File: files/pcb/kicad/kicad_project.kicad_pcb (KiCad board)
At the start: 2 copper layers, 100 x 60.5 mm, 2 parts, among them IC1 ICM7555CD, IC2 ICM7555CD

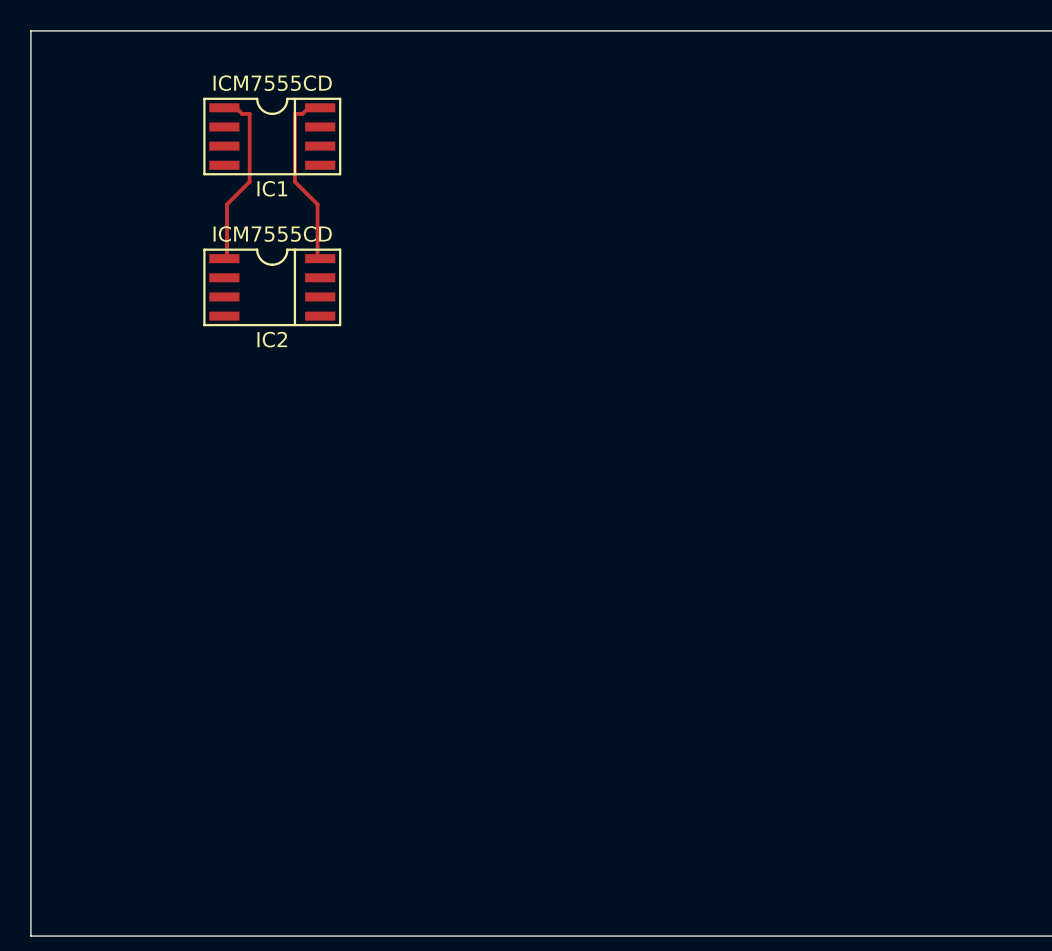
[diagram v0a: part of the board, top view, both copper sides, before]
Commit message: 回路更新
マイコン周り作成、各子階層シートを追加
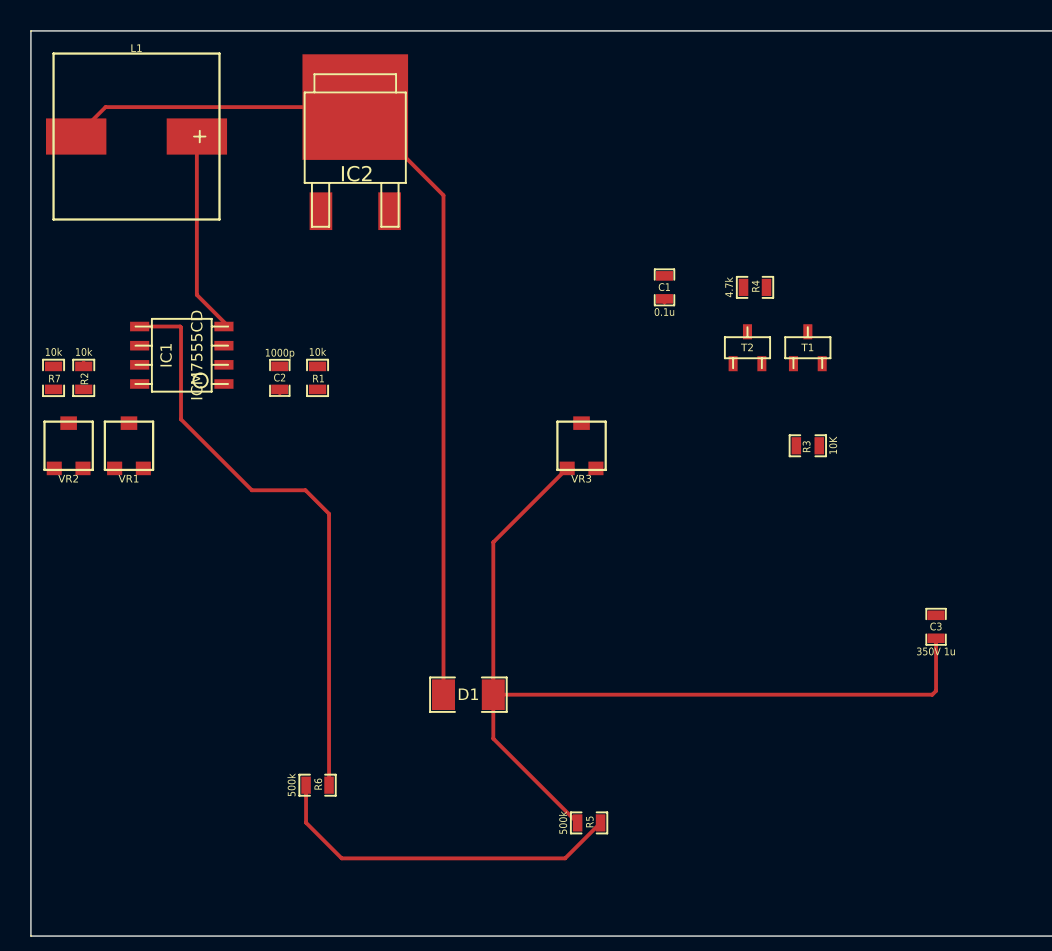
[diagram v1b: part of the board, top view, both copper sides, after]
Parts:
- added C1: 0.1u, SM0603_Capa, F.Cu at (67.0, 36.0)
- added C2: 1000p, SM0603_Capa, F.Cu at (41.5, 42.0)
- added C3: 350V 1u, SM0603_Capa, F.Cu at (85.0, 58.5)
- added D1: DIODE, SM1206, F.Cu at (54.0, 63.0)
- added L1: 220uH, smd10x10, F.Cu at (32.0, 26.0)
- added R1: 10k, SM0603_Resistor, F.Cu at (44.0, 42.0)
- added R2: 10k, SM0603_Resistor, F.Cu at (28.5, 42.0)
- added R3: 10K, SM0603_Resistor, F.Cu at (76.5, 46.5)
- added R4: 4.7k, SM0603_Resistor, F.Cu at (73.0, 36.0)
- added R5: 500k, SM0603_Resistor, F.Cu at (62.0, 71.5)
- added R6: 500k, SM0603_Resistor, F.Cu at (44.0, 69.0)
- added R7: 10k, SM0603_Resistor, F.Cu at (26.5, 42.0)
- added T1: 2SC, sot23, F.Cu at (76.5, 40.0)
- added T2: 2SA, sot23, F.Cu at (72.5, 40.0)
- added VR1: 100k, SMD_VOLUME, F.Cu at (31.5, 46.5)
- added VR2: 10k, SMD_VOLUME, F.Cu at (27.5, 46.5)
- added VR3: VOLUME, SMD_VOLUME, F.Cu at (61.5, 46.5)
- IC1: footprint ICM7555CD -> so-8
- IC2: value ICM7555CD -> FET; footprint ICM7555CD -> sot428
- moved IC1 15.7 mm to (35.0, 40.5), turned to 90 degrees
- moved IC2 10.1 mm to (46.5, 27.5)
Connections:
- IC1 pad 1: +5V -> GND
- IC1 pad 2: (no net) -> N-0000015
- IC1 pad 3: (no net) -> N-0000014
- IC1 pad 4: (no net) -> +9V
- IC1 pad 5: (no net) -> N-0000010
- IC1 pad 6: (no net) -> N-0000011
- IC1 pad 7: (no net) -> N-000009
- IC1 pad 8: N-000001 -> +9V
- IC2 pad 1: +5V -> N-000005
- IC2 pad 2: (no net) -> N-000004
- IC2 pad 3: (no net) -> GND
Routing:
- net /nixie/170V: track 0.00 -> 61.3 mm
- net N-000004: track 0.00 -> 60.8 mm
- net N-0000010: track 0.00 -> 39.7 mm
- net N-000002: track 0.00 -> 24.0 mm
- net +9V: track 0.00 -> 14.0 mm
- net N-000001: track 12.2 -> 0.00 mm
- net +5V: track 12.2 -> 0.00 mm
- net GND: track 0.00 -> 1.87 mm

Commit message: 回路図ERC途中
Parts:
- added 200k1, 200k2: N/A, SM0603, F.Cu at (125.1, 79.6)
- added C10: 1000p, SM0603_Capa, F.Cu at (125.1, 79.6)
- added C5: 25V 10u, SM1206, F.Cu at (122.0, 72.8)
- added C6, C7, C8: 0.1u, SM0603_Capa, F.Cu at (125.1, 79.6)
- added C9: 25V 10u, SM1206, F.Cu at (121.2, 75.4)
- added T3: 2SA, TO92, F.Cu at (113.1, 74.2)
- C2: value 1000p -> 10u
- C3: value 350V 1u -> 22p
- IC1: value ICM7555CD -> ATMEGA328-A
- IC2: value FET -> 3-TERMINAL_REGULATOR
- R1: value 10k -> R
- R2: value 10k -> 1k
- R3: value 10K -> 10k
- R4: value 4.7k -> R
- R5: value 500k -> R
- R6: value 500k -> 10k
- T2: value 2SA -> 2SC
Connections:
- C1 pad 1: GND -> N-0000016
- C1 pad 2: +9V -> GND
- C2 pad 1: N-0000015 -> N-0000012
- C3 pad 1: /nixie/170V -> N-000005
- D1 pad 1: N-000004 -> N-0000012
- D1 pad 2: /nixie/170V -> +5V
- IC1 pad 1: GND -> /Sheet53F8CD20/D-
- IC1 pad 2: N-0000015 -> /Sheet53F9209C/out
- IC1 pad 3: N-0000014 -> GND
- IC1 pad 4: +9V -> +5V
- IC1 pad 5: N-0000010 -> GND
- IC1 pad 6: N-0000011 -> +5V
- IC1 pad 7: N-000009 -> N-000008
- IC1 pad 8: +9V -> N-000005
- IC2 pad 1: N-000005 -> (no net)
- IC2 pad 2: N-000004 -> (no net)
- IC2 pad 3: GND -> (no net)
- L1 pad 1: +9V -> N-0000069
- L1 pad 2: N-000004 -> N-0000059
- R1 pad 1: N-000009 -> +5V
- R1 pad 2: +9V -> N-0000016
- R2 pad 1: N-0000011 -> N-0000018
- R2 pad 2: N-000009 -> N-0000012
- R3 pad 1: N-000005 -> +5V
- R3 pad 2: N-0000014 -> N-0000012
- R4 pad 1: +9V -> +5V
- R4 pad 2: N-000006 -> /Sheet53F905A8/SCL
- R5 pad 1: /nixie/170V -> +5V
- R5 pad 2: N-000002 -> /Sheet53F905A8/SDA
- R6 pad 1: N-000002 -> +5V
- R6 pad 2: N-0000010 -> N-0000046
- R7 pad 1: N-0000010 -> GND
- R7 pad 2: N-000003 -> /Sheet53F8BA4D/out
- T1 pad 1: N-0000014 -> N-0000055
- T1 pad 2: N-000006 -> N-0000065
- T1 pad 3: N-000005 -> GND
- T2 pad 1: N-0000014 -> N-0000061
- T2 pad 2: GND -> N-0000060
- T2 pad 3: N-000005 -> N-0000062
- VR1 pad 1: N-0000011 -> N-0000066
- VR1 pad 2: N-0000015 -> N-0000068
- VR1 pad 3: N-0000015 -> N-0000068
- VR2 pad 1: N-000003 -> N-0000063
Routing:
- net +5V: track 0.00 -> 74.5 mm
- net N-000004: track 60.8 -> 0.00 mm
- net N-0000012: track 0.00 -> 58.0 mm
- net /nixie/170V: track 61.3 -> 6.92 mm
- net N-0000010: track 39.7 -> 0.00 mm
- net N-000002: track 24.0 -> 0.00 mm
- net GND: track 1.87 -> 22.4 mm
- net N-0000046: track 0.00 -> 18.0 mm
- net +9V: track 14.0 -> 0.00 mm
- net N-0000069: track 0.00 -> 10.5 mm
- net N-000005: track 0.30 -> 3.96 mm
- net /Sheet53F905A8/SDA: track 0.00 -> 3.32 mm
- net N-0000059: track 0.00 -> 2.76 mm

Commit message: 部品リスト完了、PCBに部品を配置
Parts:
- removed 200k1, 200k2: N/A, SM0603
- removed VR3: VOLUME, SMD_VOLUME
- added C11: 25V 10u, SM0805, F.Cu at (256.0, 133.0)
- added C12: 1000p, SM0603_Capa, F.Cu at (229.5, 171.0)
- added C13: 350V 1u, my_SMD5750, F.Cu at (214.5, 124.0)
- added C14: 5.5V 0.1F, my_double_layer_capacitor, F.Cu at (210.5, 151.5)
- added C15: 0.1u, SM0603_Capa, F.Cu at (231.0, 180.0)
- added C16: 0.1u, SM0603_Capa, F.Cu at (231.0, 163.0)
- added C17: 0.1u, SM0603_Capa, F.Cu at (245.0, 179.5)
- added C18: 0.1u, SM0603_Capa, F.Cu at (253.0, 185.0)
- added C19: 0.1u, SM0603_Capa, F.Cu at (236.0, 180.0)
- added C4: 22p, SM0603_Capa, F.Cu at (236.0, 177.5)
- added CON1: USB_MINI_B, my_usb_mini_b, F.Cu at (163.0, 111.5)
- added D2: DIODE, SM1206POL, F.Cu at (232.5, 125.0)
- added D3: DIODE, SM0805, F.Cu at (249.0, 175.0)
- added D4: DIODE, SM0805, F.Cu at (160.0, 118.5)
- added D5: DIODE, SM0805, F.Cu at (242.5, 151.0)
- added F1: FUSE, SM1206, F.Cu at (223.5, 134.5)
- added IC10: FET, my_sot428, F.Cu at (241.5, 122.0)
- added IC11: DS1307, so-8, F.Cu at (245.5, 133.0)
- added IC12: IC_8PIN, my_dip8, F.Cu at (192.5, 118.5)
- added IC13: AM2321, my_am2321, F.Cu at (202.0, 131.5)
- added IC3: IC_4PIN, my_dip4, F.Cu at (209.0, 167.0)
- added IC4: IC_4PIN, my_dip4, F.Cu at (211.5, 181.5)
- added IC5: SN74141_K155NA, my_dip16, F.Cu at (172.0, 172.0)
- added IC6: TLP627-4, my_dip16, F.Cu at (195.0, 178.0)
- added IC7: TLP627-4, my_dip16, F.Cu at (172.0, 178.0)
- added IC8: MY_3_TERMINAL_REGULATOR, my_SOT223, F.Cu at (226.5, 118.0)
- added IC9: ICM7555CD, so-8, F.Cu at (219.5, 103.5)
- added K1: CONN_3, my_3pin, F.Cu at (199.5, 188.5)
- added K2: CONN_3, my_3pin, F.Cu at (190.0, 189.0)
- added K3: CONN_3, my_3pin, F.Cu at (241.5, 184.5)
- added K4: CONN_3, my_3pin, F.Cu at (236.5, 185.5)
- added P1: CONN_6, my_connector_6, F.Cu at (196.5, 144.5)
- added PD1: PHOTO_DIODE, my_photo_diode, F.Cu at (226.0, 127.0)
- added R10: 500k, SM0805, F.Cu at (241.5, 176.5)
- added R11: 10k, SM0805, F.Cu at (237.0, 155.5)
- added R12: 10k, SM0805, F.Cu at (223.5, 148.0)
- added R13: 10k, SM0805, F.Cu at (219.0, 145.0)
- added R14: 10k, SM0805, F.Cu at (220.5, 115.5)
- added R15: 10K, SM0805, F.Cu at (247.5, 146.5)
- added R16: 4.7k, SM0805, F.Cu at (230.0, 158.5)
- added R17: 500k, SM0805, F.Cu at (232.0, 167.0)
- added R18: 500k, SM0805, F.Cu at (235.5, 172.5)
- added R19: 10k, SM0805, F.Cu at (251.5, 153.0)
- added R20: 68, SM0805, F.Cu at (191.5, 153.0)
- added R21: 68, SM0805, F.Cu at (165.0, 128.0)
- added R22: 2K, SM0805, F.Cu at (172.0, 117.5)
- added R23: NC, SM0805, F.Cu at (222.0, 154.5)
- added R24: 10k, SM0805, F.Cu at (217.5, 164.5)
- added R25: 10k, SM0805, F.Cu at (249.5, 178.0)
- added R26: 10k, SM0805, F.Cu at (249.0, 180.5)
- added R27: 3.3k, SM0805, F.Cu at (231.0, 174.5)
- added R28: 7.5k, SM0805, F.Cu at (237.5, 175.0)
- added R29: 10k, SM0805, F.Cu at (236.5, 162.5)
- added R30: N/A, SM0805, F.Cu at (200.5, 181.0)
- added R31: N/A, SM0805, F.Cu at (225.5, 165.0)
- added R8: 10k, SM0805, F.Cu at (237.5, 150.0)
- added R9: 500k, SM0805, F.Cu at (222.0, 167.5)
- added SW1: SW_PUSH, my_tact_switch, F.Cu at (205.5, 115.5)
- added SW2: EVQWK, my_rotary_switch, F.Cu at (180.0, 156.5)
- added SW3: SW_PUSH, my_tact_switch, F.Cu at (196.0, 115.5)
- added SW4: SW_PUSH, my_tact_switch, F.Cu at (187.0, 115.5)
- added SW5: SW_PUSH, my_tact_switch, F.Cu at (177.5, 115.5)
- added U1: NEON, my_neon, F.Cu at (190.0, 192.0)
- added U10: NIXIE_IN_16, my_nixie, F.Cu at (181.5, 196.0)
- added U11: DC_JACK, my_dcjack, F.Cu at (161.5, 156.5)
- added U12: LOAD, my_sounder, F.Cu at (248.0, 165.5)
- added U13: remocon, my_remocon, F.Cu at (181.5, 123.0)
- added U14: napion, my_napion, F.Cu at (169.5, 121.0)
- added U2: NEON, my_neon, F.Cu at (195.0, 182.5)
- added U3: NEON, my_neon, F.Cu at (232.0, 186.0)
- added U4: NEON, my_neon, F.Cu at (228.5, 184.0)
- added U5: NIXIE_IN_16, my_nixie, F.Cu at (243.5, 196.0)
- added U6: NIXIE_IN_16, my_nixie, F.Cu at (213.5, 196.5)
- added U7: NIXIE_IN_16, my_nixie, F.Cu at (166.5, 196.0)
- added U8: NIXIE_IN_16, my_nixie, F.Cu at (229.0, 196.5)
- added U9: NIXIE_IN_16, my_nixie, F.Cu at (198.0, 196.5)
- added X1: 12MHz, my_crystal, F.Cu at (190.0, 163.0)
- added X2: 32.768kHz, my_crystal_32p768, F.Cu at (223.0, 182.5)
- C10: value 1000p -> 0.1u
- C2: value 10u -> 0.1u
- C3: value 22p -> 10u; footprint SM0603_Capa -> SM0805
- C5: value 25V 10u -> 22p; footprint SM1206 -> SM0603_Capa
- C7: value 0.1u -> 25V 10u; footprint SM0603_Capa -> SM0805
- C9: value 25V 10u -> 0.1u; footprint SM1206 -> SM0603_Capa
- D1: footprint SM1206 -> SM0805
- IC1: footprint so-8 -> TQFP32
- IC2: value 3-TERMINAL_REGULATOR -> IC_16PIN; footprint sot428 -> my_so16
- L1: footprint smd10x10 -> my_inductor
- R1: value R -> 510; footprint SM0603_Resistor -> SM0805
- R2, R3, R7: footprint SM0603_Resistor -> SM0805
- R4, R5: value R -> 10k; footprint SM0603_Resistor -> SM0805
- R6: value 10k -> 330; footprint SM0603_Resistor -> SM0805
- T1, T2: footprint sot23 -> SOT23
- T3: footprint TO92 -> SOT23
- VR1, VR2: footprint SMD_VOLUME -> my_SMD_VR
- moved R2 233.6 mm to (219.5, 176.5), turned to 0 degrees
- moved C2 233.5 mm to (237.5, 169.0), turned to 0 degrees
- moved R7 231.2 mm to (219.0, 170.0), turned to 180 degrees
- moved R6 226.6 mm to (244.5, 174.5), turned to 180 degrees
- moved VR2 224.5 mm to (235.5, 131.0), turned to 90 degrees
- moved R1 217.1 mm to (231.5, 151.5), turned to 0 degrees
- moved L1 212.0 mm to (228.5, 105.5), turned to 90 degrees
- moved D1 205.8 mm to (227.0, 174.5)
- moved IC2 203.7 mm to (191.5, 170.5), turned to 180 degrees
- moved IC1 202.8 mm to (198.5, 160.5), turned to 0 degrees
- moved C1 200.2 mm to (234.0, 146.5), turned to 0 degrees
- moved VR1 196.9 mm to (217.5, 111.0)
- moved R3 193.8 mm to (225.0, 171.0)
- moved R4 187.7 mm to (225.5, 145.5)
- moved T1 173.7 mm to (231.5, 118.5)
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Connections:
- C1 pad 1: N-0000016 -> N-0000018
- C10 pad 1: N-0000068 -> GND
- C10 pad 2: GND -> N-0000063
- C2 pad 1: N-0000012 -> +5V
- C3 pad 1: N-000005 -> N-000004
- C5 pad 1: N-0000069 -> N-000003
- C6 pad 1: N-0000069 -> GND
- C6 pad 2: GND -> +5V
- C7 pad 1: +5V -> N-0000063
- C8 pad 1: GND -> N-0000063
- C8 pad 2: N-0000069 -> GND
- D1 pad 1: N-0000012 -> N-000004
- IC1 pad 7: N-000008 -> N-000003
- IC1 pad 8: N-000005 -> N-0000011
- IC2 pad 1: (no net) -> /PB0
- IC2 pad 2: (no net) -> /PB1
- IC2 pad 3: (no net) -> /PB2
- L1 pad 1: N-0000069 -> N-0000063
- R1 pad 2: N-0000016 -> N-0000018
- R2 pad 1: N-0000018 -> /RESET
- R2 pad 2: N-0000012 -> N-000004
- R3 pad 2: N-0000012 -> N-000004
- R7 pad 1: GND -> +5V
- R7 pad 2: /Sheet53F8BA4D/out -> N-0000026
- VR1 pad 2: N-0000068 -> N-0000055
- VR1 pad 3: N-0000068 -> N-0000055
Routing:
- net +5V: track 74.5 -> 0.00 mm
- net N-0000012: track 58.0 -> 0.00 mm
- net GND: track 22.4 -> 0.00 mm
- net N-0000047: track 18.0 -> 0.00 mm
- net N-0000069: track 10.5 -> 0.00 mm
- net /nixie/170V: track 6.92 -> 0.00 mm
- net N-000005: track 3.96 -> 0.00 mm
- net /Sheet53F905A8/SDA: track 3.32 -> 0.00 mm
- net N-0000062: track 2.76 -> 0.00 mm
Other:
- board size 100 x 60.5 mm -> 100 x 99 mm

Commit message: PCB更新
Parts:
- added U15: MY_PIN52, my_pin52, F.Cu at (255.0, 118.0)
- added U16: MY_PIN52, my_pin52, F.Cu at (163.5, 148.0)
- added U17: MY_PIN52, my_pin52, F.Cu at (164.0, 118.5)
- added U18: MY_PIN52, my_pin52, F.Cu at (255.0, 148.5)
- added my_drill_3mm: VAL**, my_drill_3mm, F.Cu at (162.5, 130.5)
- added my_drill_3mm: VAL**, my_drill_3mm, F.Cu at (162.0, 106.0)
- added my_drill_3mm: VAL**, my_drill_3mm, F.Cu at (256.5, 131.0)
- added my_drill_3mm: VAL**, my_drill_3mm, F.Cu at (256.5, 106.5)
- added my_drill_3mm: VAL**, my_drill_3mm, F.Cu at (256.0, 138.5)
- added my_drill_3mm: VAL**, my_drill_3mm, F.Cu at (256.0, 159.5)
- added my_drill_3mm: VAL**, my_drill_3mm, F.Cu at (162.0, 157.5)
- added my_drill_3mm: VAL**, my_drill_3mm, F.Cu at (162.0, 138.0)
- IC12: value IC_8PIN -> LPS331AP
- moved U1 100.6 mm to (185.0, 91.5)
- moved K2 100.3 mm to (166.5, 91.5)
- moved U3 97.6 mm to (214.5, 90.0)
- moved K4 96.0 mm to (223.0, 90.5)
- moved U4 95.3 mm to (207.5, 91.0)
- moved U2 93.5 mm to (178.5, 90.5)
- moved U12 87.3 mm to (179.0, 112.0)
- moved D4 70.0 mm to (225.0, 144.5), turned to 270 degrees
- moved X2 61.5 mm to (197.5, 126.5), turned to 90 degrees
- moved R21 61.0 mm to (222.5, 148.5)
- moved F1 57.2 mm to (169.5, 153.5), turned to 270 degrees
- moved R22 57.1 mm to (220.0, 148.5)
- moved IC2 54.2 mm to (245.5, 165.5)
- moved X1 48.7 mm to (207.5, 117.5)
- moved C8 47.5 mm to (242.0, 139.5), turned to 270 degrees
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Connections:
- K2 pad 1: N-0000082 -> N-00000121
- K4 pad 1: N-0000079 -> N-00000118
- R30 pad 1: N-0000082 -> /nixie/Sheet53F9F7BA/colon_l
- R31 pad 1: N-0000079 -> /nixie/Sheet53F9F7BA/colon_r
- U1 pad 2: N-0000082 -> N-00000121
- U2 pad 2: N-0000082 -> N-00000121
- U3 pad 2: N-0000079 -> N-00000118
- U4 pad 2: N-0000079 -> N-00000118
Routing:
- net +5V: track 0.00 -> 264.3 mm, vias 0 -> 5
- net GND: track 0.00 -> 258.3 mm, vias 0 -> 5
- net /nixie/Sheet53F9F7BA/dot_cathode_r: track 0.00 -> 180.5 mm
- net N-0000091: track 0.00 -> 124.6 mm, vias 0 -> 4
- net /nixie/Sheet53F9F7BA/dot_cathode_l: track 0.00 -> 107.9 mm
- net /nixie/N9: track 0.00 -> 106.7 mm, vias 0 -> 2
- net /nixie/N2: track 0.00 -> 100.4 mm, vias 0 -> 4
- net /nixie/N7: track 0.00 -> 90.0 mm, vias 0 -> 2
- net /nixie/N1: track 0.00 -> 85.5 mm, vias 0 -> 1
- net /nixie/N4: track 0.00 -> 81.5 mm, vias 0 -> 2
- net /nixie/N0: track 0.00 -> 76.5 mm
- net /nixie/N3: track 0.00 -> 76.0 mm, vias 0 -> 1
- net /nixie/N8: track 0.00 -> 76.0 mm
- net /nixie/N5: track 0.00 -> 69.6 mm, vias 0 -> 1
- net /Sheet53F9209C/out: track 0.00 -> 60.0 mm, vias 0 -> 2
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- added copper zone on B.Cu, net GND
- added copper zone on F.Cu, net GND
- added copper zone on B.Cu, net N-00000117
- added copper zone on F.Cu, net N-00000117
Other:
- board size 100 x 99 mm -> 100 x 102 mm

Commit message: PCB
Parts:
- removed my_drill_3mm (x8): VAL**, my_drill_3mm
- added my_M3_screw: VAL**, my_M3_screw, F.Cu at (257.6, 181.5)
- added my_M3_screw: VAL**, my_M3_screw, F.Cu at (257.5, 109.6)
- added my_M3_screw: VAL**, my_M3_screw, F.Cu at (164.5, 109.6)
- added my_M3_screw: VAL**, my_M3_screw, F.Cu at (164.6, 181.5)
- added my_M3_screw: VAL**, my_M3_screw, F.Cu at (164.5, 141.6)
- added my_M3_screw: VAL**, my_M3_screw, F.Cu at (257.5, 141.6)
- C1, C10, C12, C15, C16, C17, C18, C19, C2, C3, C4, C5, C6, D1, D2, D5, IC2, R1, R10, R12, R13, R14, R15, R16, R17, R18, R19, R2, R24, R25, R26, R27, R28, R29, R3, R30, R31, R4, R5, R6, R7, R8, R9, X1: moved to B.Cu
- IC12: footprint my_dip8 -> my_dip_module
- moved U17 93.5 mm to (257.5, 119.6)
- moved U15 90.5 mm to (164.5, 119.6)
- moved C18 76.3 mm to (189.5, 121.6)
- moved U14 74.1 mm to (247.9, 121.5)
- moved R24 71.1 mm to (173.1, 113.3), turned to 270 degrees
- moved R23 69.6 mm to (180.4, 147.1)
- moved C9 67.8 mm to (178.9, 158.5), turned to 0 degrees
- moved R26 66.8 mm to (175.6, 113.3)
- moved C8 66.7 mm to (178.9, 161.0), turned to 0 degrees
- moved R25 62.6 mm to (178.1, 113.3)
- moved C11 62.0 mm to (178.9, 156.5), turned to 0 degrees
- moved IC12 60.8 mm to (235.2, 113.7), turned to 270 degrees
- moved R4 56.7 mm to (198.0, 124.8), turned to 270 degrees
- moved R28 56.7 mm to (187.5, 121.6), turned to 270 degrees
- moved IC8 56.5 mm to (171.9, 158.5), turned to 90 degrees
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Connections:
- C10 pad 1: GND -> GND_L
- C11 pad 1: +5V -> 5V_L
- C11 pad 2: GND -> GND_L
- C12 pad 2: GND -> GND_L
- C13 pad 2: GND -> GND_L
- C14 pad 1: N-00000113 -> CLK_PW_L
- C15 pad 2: GND -> GND_L
- C6 pad 1: GND -> GND_L
- C7 pad 2: GND -> GND_L
- C8 pad 2: GND -> GND_L
- C9 pad 1: +5V -> 5V_L
- C9 pad 2: GND -> GND_L
- D5 pad 2: N-00000113 -> CLK_PW_H
- IC10 pad 3: GND -> GND_L
- IC11 pad 3: N-00000113 -> CLK_PW_H
- IC2 pad 1: /PB0 -> /PB_P0
- IC2 pad 10: N-0000074 -> /nixie/L3
- IC2 pad 11: N-0000073 -> /nixie/L4
- IC2 pad 12: N-0000069 -> /nixie/L5
- IC2 pad 13: N-0000072 -> /nixie/L6
- IC2 pad 14: N-0000071 -> /nixie/L7
- IC2 pad 15: N-0000070 -> /nixie/L8
- IC2 pad 2: /PB1 -> /PB_P1
- IC2 pad 3: /PB2 -> /PB_P2
- IC2 pad 4: GND -> GND_L
- IC2 pad 5: GND -> GND_L
- IC2 pad 6: GND -> GND_L
- IC2 pad 7: N-0000068 -> /nixie/L1
- IC2 pad 8: GND -> GND_L
- IC2 pad 9: N-0000075 -> /nixie/L2
- IC3 pad 2: /MOSI -> /PB_P3
- IC4 pad 2: /MISO -> /PB_P4
- IC5 pad 12: GND -> GND_L
- IC5 pad 3: /PC3 -> /PC_P3
- IC5 pad 4: /PC2 -> /PC_P2
- IC5 pad 6: /PC1 -> /PC_P1
- IC5 pad 7: /PC0 -> /PC_P0
- IC6 pad 2: N-0000070 -> /nixie/L1
- IC6 pad 4: N-0000071 -> /nixie/L2
- IC6 pad 6: N-0000072 -> /nixie/L3
- IC6 pad 8: N-0000069 -> /nixie/L4
- IC7 pad 2: N-0000073 -> /nixie/L5
- IC7 pad 4: N-0000074 -> /nixie/L6
- IC7 pad 6: N-0000075 -> /nixie/L7
- IC7 pad 8: N-0000068 -> /nixie/L8
- IC8 pad 2: GND -> GND_L
- IC8 pad 3: +5V -> 5V_L
- IC9 pad 1: GND -> GND_L
- R10 pad 2: GND -> GND_L
- R27 pad 1: +5V -> 5V_L
- R30 pad 2: GND -> GND_L
- R31 pad 2: GND -> GND_L
- R9 pad 2: GND -> GND_L
- T1 pad 3: GND -> GND_L
- T3 pad 2: GND -> GND_L
- U11 pad 3: GND -> GND_L
- U15 pad 1: (no net) -> CLK_PW_H
- U15 pad 10: (no net) -> +5V
- U15 pad 2: (no net) -> GND
- U15 pad 3: (no net) -> GND
- U15 pad 4: (no net) -> GND
- U15 pad 5: (no net) -> GND
- U15 pad 6: (no net) -> /PC3
- U15 pad 7: (no net) -> /PC2
- U15 pad 8: (no net) -> /PC1
- U15 pad 9: (no net) -> /PC0
- U16 pad 1: (no net) -> CLK_PW_L
- U16 pad 10: (no net) -> 5V_L
- U16 pad 2: (no net) -> GND_L
- U16 pad 3: (no net) -> GND_L
- U16 pad 4: (no net) -> GND_L
- U16 pad 5: (no net) -> GND_L
- U16 pad 6: (no net) -> /PC_P3
- U16 pad 7: (no net) -> /PC_P2
- U16 pad 8: (no net) -> /PC_P1
- U16 pad 9: (no net) -> /PC_P0
- U17 pad 1: (no net) -> /PB0
- U17 pad 10: (no net) -> GND
- U17 pad 2: (no net) -> /PB1
- U17 pad 3: (no net) -> /PB2
- U17 pad 4: (no net) -> /MOSI
- U17 pad 5: (no net) -> /MISO
- U17 pad 6: (no net) -> GND
- U17 pad 7: (no net) -> GND
- U17 pad 8: (no net) -> GND
- U17 pad 9: (no net) -> GND
- U18 pad 1: (no net) -> /PB_P0
- U18 pad 10: (no net) -> GND_L
- U18 pad 2: (no net) -> /PB_P1
- U18 pad 3: (no net) -> /PB_P2
- U18 pad 4: (no net) -> /PB_P3
- U18 pad 5: (no net) -> /PB_P4
- U18 pad 6: (no net) -> GND_L
- U18 pad 7: (no net) -> GND_L
- U18 pad 8: (no net) -> GND_L
- U18 pad 9: (no net) -> GND_L
- VR2 pad 2: GND -> GND_L
- VR2 pad 3: GND -> GND_L
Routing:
- net GND_L: track 0.00 -> 192.4 mm, vias 0 -> 8
- net /nixie/N0: track 76.5 -> 199.0 mm, vias 0 -> 10
- net /nixie/N1: track 85.5 -> 184.7 mm, vias 1 -> 13
- net (no net): track 0.00 -> 95.3 mm, vias 0 -> 3
- net /nixie/Sheet53F9F7BA/dot_cathode_l: track 107.9 -> 197.8 mm, vias 0 -> 7
- net /Sheet53F8FD69/A: track 11.9 -> 96.7 mm, vias 1 -> 7
- net /nixie/N2: track 100.4 -> 180.0 mm, vias 4 -> 9
- net /nixie/Sheet53F9F7BA/3: track 5.85 -> 81.7 mm, vias 0 -> 9
- net +5V: track 264.3 -> 190.2 mm, vias 5 -> 11
- net N-0000078: track 124.6 -> 50.9 mm, vias 4 -> 2
- net /PB_P3: track 0.00 -> 62.9 mm, vias 0 -> 3
- net /PC0: track 0.00 -> 59.3 mm, vias 0 -> 2
- net N-0000055: track 55.6 -> 112.0 mm, vias 0 -> 3
- net /PC1: track 0.00 -> 55.9 mm, vias 0 -> 4
- net N-0000063: track 53.6 -> 3.47 mm, vias 1 -> 0
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- removed copper zone on B.Cu, net N-00000101
- removed copper zone on F.Cu, net N-00000101
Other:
- board size 100 x 102 mm -> 100 x 96 mm
